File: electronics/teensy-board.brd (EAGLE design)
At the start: 50.5 x 73.7 mm, 21 parts

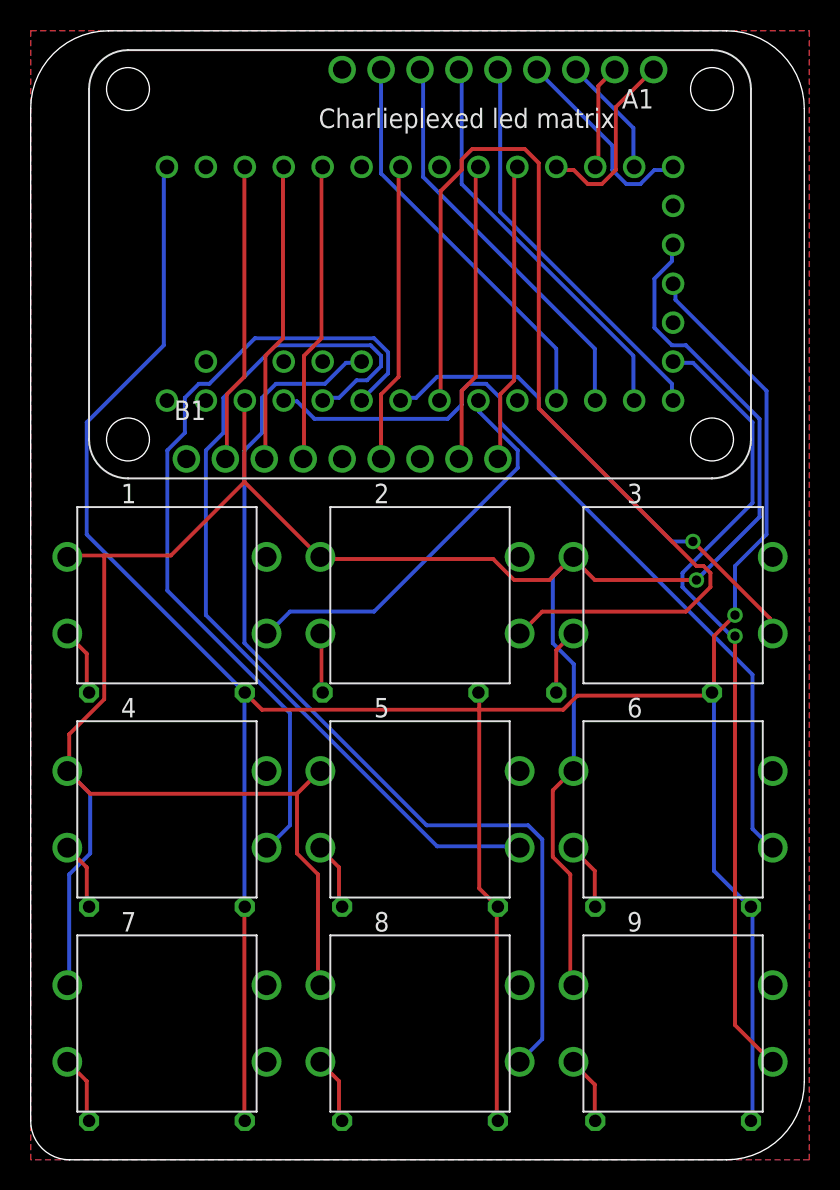
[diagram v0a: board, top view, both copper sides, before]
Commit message: fixed flipped charlieplexed led
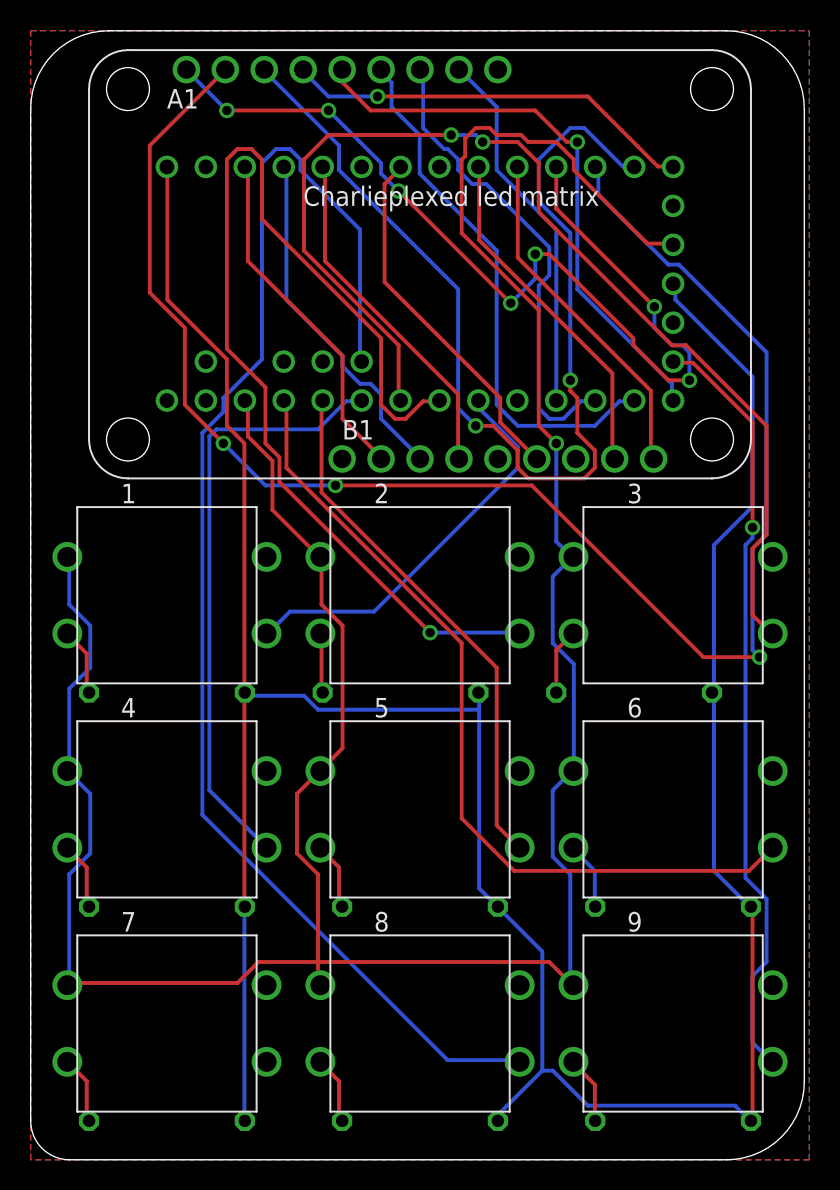
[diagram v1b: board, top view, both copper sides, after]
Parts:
- turned LED to 270 degrees
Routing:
- net A2: track 6.97 -> 106.7 mm, vias 0 -> 3
- net A3: track 7.93 -> 68.8 mm, vias 0 -> 2
- net A1: track 12.4 -> 63.4 mm, vias 0 -> 7
- net S3: track 32.8 -> 73.4 mm, vias 1 -> 2
- net S8: track 63.8 -> 89.5 mm
- net S5: track 58.8 -> 34.6 mm
- net 3.3: track 171.2 -> 185.6 mm
- net S4: track 52.9 -> 39.3 mm
- net A4: track 13.4 -> 26.8 mm, vias 0 -> 1
- net A5: track 26.3 -> 37.2 mm, vias 0 -> 1
- net A6: track 26.3 -> 35.2 mm
- net A7: track 26.3 -> 31.0 mm
- net N$6: track 19.6 -> 23.6 mm
- net N$3: track 19.6 -> 23.1 mm
- net GND: track 188.5 -> 185.0 mm, vias 1 -> 0
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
